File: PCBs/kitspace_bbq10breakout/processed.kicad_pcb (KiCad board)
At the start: 2 copper layers, 16.5 x 21.6 mm, 4 parts, among them J1 Conn_01x08, J2 Conn_01x08, U1 BBQ10KBD

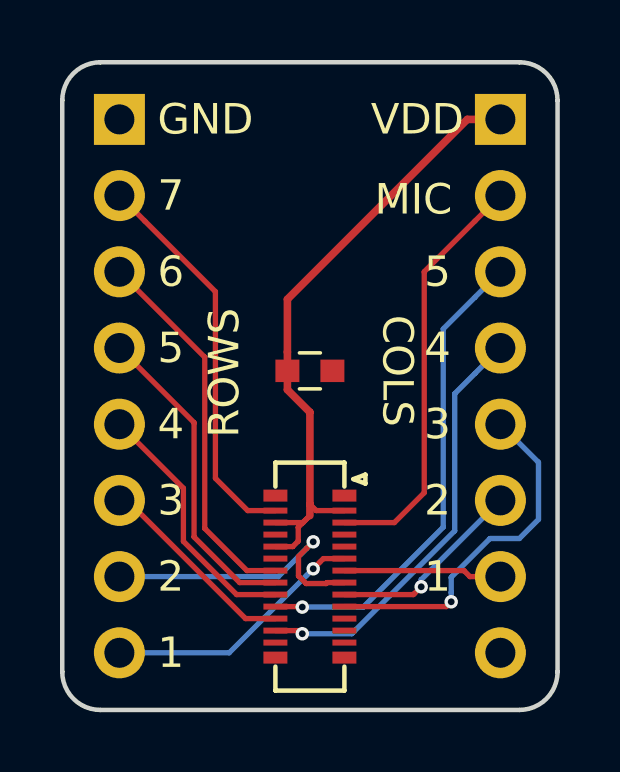
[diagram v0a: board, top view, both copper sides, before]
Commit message: recheck all circuits and clean up fill zone by rerouting the nets using freerouting and manually
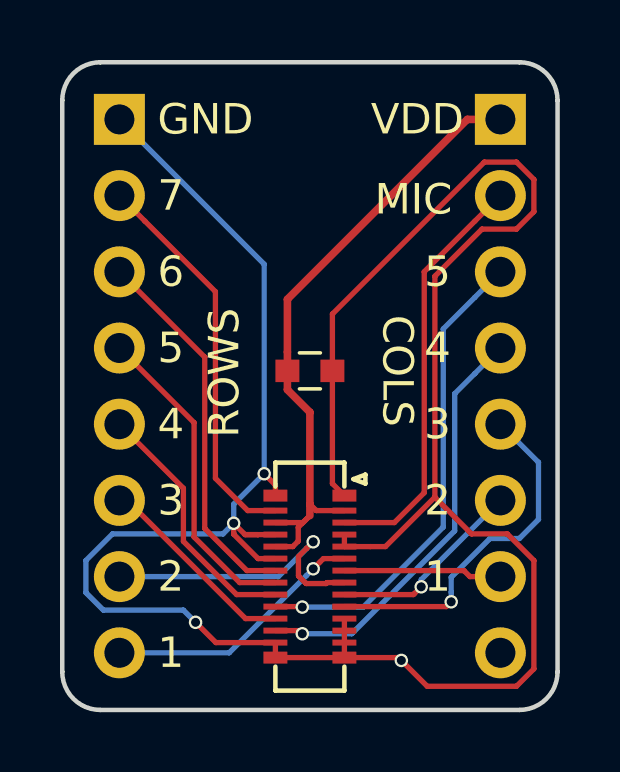
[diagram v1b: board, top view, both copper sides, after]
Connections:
- C1 pad 2: (no net) -> GND
- J1 pad 1: (no net) -> GND
- J2 pad 8: (no net) -> Net-(J2-Pad8)
- U1 pad 1: (no net) -> GND
- U1 pad 11: (no net) -> GND
- U1 pad 12: (no net) -> GND
- U1 pad 13: (no net) -> GND
- U1 pad 14: (no net) -> GND
- U1 pad 15: (no net) -> GND
- U1 pad 16: (no net) -> GND
- U1 pad 23: (no net) -> GND
- U1 pad 25: (no net) -> GND
- U1 pad 28: (no net) -> GND
- U1 pad 4: (no net) -> GND
- U1 pad 5: (no net) -> GND
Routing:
- net GND: track 0.00 -> 85.2 mm, vias 0 -> 4
